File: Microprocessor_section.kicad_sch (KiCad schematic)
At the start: 17 parts, among them J9 Conn_01x04_Male, Q4 SS8050, Q5 SS8050, SW1 K2-1102SP-C4SC-04, U4 CH340C, U5 ESP32-WROOM-32D

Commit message: I was never here
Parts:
- renumbered R19 to R20, R20 to R21, R21 to R22, R22 to R23
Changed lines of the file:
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@@
   (symbol (lib_id "power:+3V3") (at 158.75 43.18 0) (unit 1)
     (in_bom yes) (on_board yes)
-    (property "Reference" "#PWR057" (id 0) (at 158.75 46.99 0)
+    (property "Reference" "#PWR058" (id 0) (at 158.75 46.99 0)
       (effects (font (size 1.27 1.27)) hide)
     )
@@
   (symbol (lib_id "power:+3V3") (at 140.97 58.42 0) (mirror y) (unit 1)
     (in_bom yes) (on_board yes)
-    (property "Reference" "#PWR055" (id 0) (at 140.97 62.23 0)
+    (property "Reference" "#PWR056" (id 0) (at 140.97 62.23 0)
       (effects (font (size 1.27 1.27)) hide)
     )
@@
   (symbol (lib_id "Device:R") (at 140.97 64.77 0) (unit 1)
     (in_bom yes) (on_board yes)
-    (property "Reference" "R22" (id 0) (at 142.748 63.6016 0)
+    (property "Reference" "R23" (id 0) (at 142.748 63.6016 0)
       (effects (font (size 1.27 1.27)) (justify left))
     )
@@
   (symbol (lib_id "power:GND") (at 158.75 60.96 0) (unit 1)
     (in_bom yes) (on_board yes)
-    (property "Reference" "#PWR058" (id 0) (at 158.75 67.31 0)
+    (property "Reference" "#PWR059" (id 0) (at 158.75 67.31 0)
       (effects (font (size 1.27 1.27)) hide)
     )
@@
   (symbol (lib_id "power:GND") (at 149.86 83.82 0) (unit 1)
     (in_bom yes) (on_board yes)
-    (property "Reference" "#PWR056" (id 0) (at 149.86 90.17 0)
+    (property "Reference" "#PWR057" (id 0) (at 149.86 90.17 0)
       (effects (font (size 1.27 1.27)) hide)
     )
@@
   (symbol (lib_id "power:+3V3") (at 33.02 166.37 0) (unit 1)
     (in_bom yes) (on_board yes)
-    (property "Reference" "#PWR047" (id 0) (at 33.02 170.18 0)
+    (property "Reference" "#PWR048" (id 0) (at 33.02 170.18 0)
       (effects (font (size 1.27 1.27)) hide)
     )
@@
   (symbol (lib_id "power:GND") (at 78.74 186.69 0) (unit 1)
     (in_bom yes) (on_board yes)
-    (property "Reference" "#PWR054" (id 0) (at 78.74 193.04 0)
+    (property "Reference" "#PWR055" (id 0) (at 78.74 193.04 0)
       (effects (font (size 1.27 1.27)) hide)
     )
@@
   (symbol (lib_id "Device:R") (at 33.02 180.34 0) (mirror x) (unit 1)
     (in_bom yes) (on_board yes)
-    (property "Reference" "R19" (id 0) (at 34.798 181.5084 0)
+    (property "Reference" "R20" (id 0) (at 34.798 181.5084 0)
       (effects (font (size 1.27 1.27)) (justify left))
     )
@@
   (symbol (lib_id "power:GND") (at 33.02 186.69 0) (unit 1)
     (in_bom yes) (on_board yes)
-    (property "Reference" "#PWR048" (id 0) (at 33.02 193.04 0)
+    (property "Reference" "#PWR049" (id 0) (at 33.02 193.04 0)
       (effects (font (size 1.27 1.27)) hide)
     )
@@
   (symbol (lib_id "power:GND") (at 177.8 137.16 0) (unit 1)
     (in_bom yes) (on_board yes)
-    (property "Reference" "#PWR059" (id 0) (at 177.8 143.51 0)
+    (property "Reference" "#PWR060" (id 0) (at 177.8 143.51 0)
       (effects (font (size 1.27 1.27)) hide)
     )
@@
   (symbol (lib_id "power:GND") (at 39.37 88.9 0) (unit 1)
     (in_bom yes) (on_board yes) (fields_autoplaced)
-    (property "Reference" "#PWR049" (id 0) (at 39.37 95.25 0)
+    (property "Reference" "#PWR050" (id 0) (at 39.37 95.25 0)
       (effects (font (size 1.27 1.27)) hide)
     )
@@
   (symbol (lib_id "power:GND") (at 64.77 101.6 0) (unit 1)
     (in_bom yes) (on_board yes) (fields_autoplaced)
-    (property "Reference" "#PWR053" (id 0) (at 64.77 107.95 0)
+    (property "Reference" "#PWR054" (id 0) (at 64.77 107.95 0)
       (effects (font (size 1.27 1.27)) hide)
     )
@@
   (symbol (lib_id "Device:R") (at 95.25 102.87 90) (unit 1)
     (in_bom yes) (on_board yes) (fields_autoplaced)
-    (property "Reference" "R21" (id 0) (at 95.25 98.1542 90))
+    (property "Reference" "R22" (id 0) (at 95.25 98.1542 90))
     (property "Value" "12k" (id 1) (at 95.25 100.6911 90))
     (property "Footprint" "Resistor_SMD:R_0603_1608Metric" (id 2) (at 95.25 104.648 90)
@@
   (symbol (lib_id "power:+3V3") (at 48.26 91.44 0) (unit 1)
     (in_bom yes) (on_board yes) (fields_autoplaced)
-    (property "Reference" "#PWR050" (id 0) (at 48.26 95.25 0)
+    (property "Reference" "#PWR051" (id 0) (at 48.26 95.25 0)
       (effects (font (size 1.27 1.27)) hide)
     )
@@
   (symbol (lib_id "power:GND") (at 48.26 101.6 0) (unit 1)
     (in_bom yes) (on_board yes) (fields_autoplaced)
-    (property "Reference" "#PWR051" (id 0) (at 48.26 107.95 0)
+    (property "Reference" "#PWR052" (id 0) (at 48.26 107.95 0)
       (effects (font (size 1.27 1.27)) hide)
     )
@@
   (symbol (lib_id "Device:R") (at 95.25 81.28 90) (unit 1)
     (in_bom yes) (on_board yes) (fields_autoplaced)
-    (property "Reference" "R20" (id 0) (at 95.25 76.5642 90))
+    (property "Reference" "R21" (id 0) (at 95.25 76.5642 90))
     (property "Value" "12k" (id 1) (at 95.25 79.1011 90))
     (property "Footprint" "Resistor_SMD:R_0603_1608Metric" (id 2) (at 95.25 83.058 90)
@@
   (symbol (lib_id "power:+3V3") (at 62.23 66.04 0) (unit 1)
     (in_bom yes) (on_board yes) (fields_autoplaced)
-    (property "Reference" "#PWR052" (id 0) (at 62.23 69.85 0)
-      (effects (font (size 1.27 1.27)) hide)
-    )
+    (property "Reference" "#PWR053" (id 0) (at 62.23 69.85 0)
+      (effects (font (size 1.27 1.27)) hide)
+    )

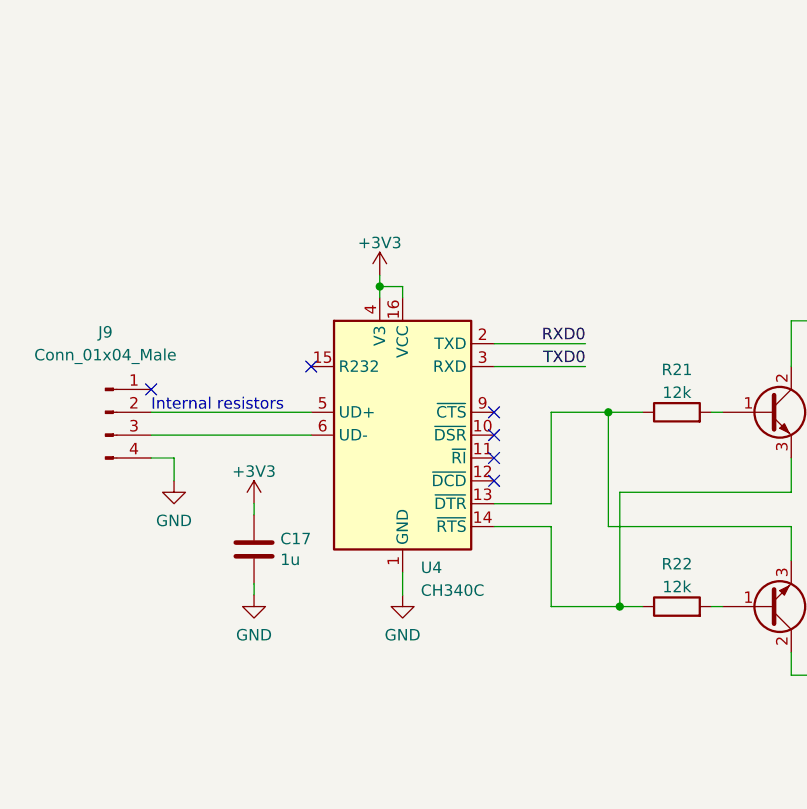
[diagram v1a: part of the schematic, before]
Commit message: Finish routing PCB revision 2
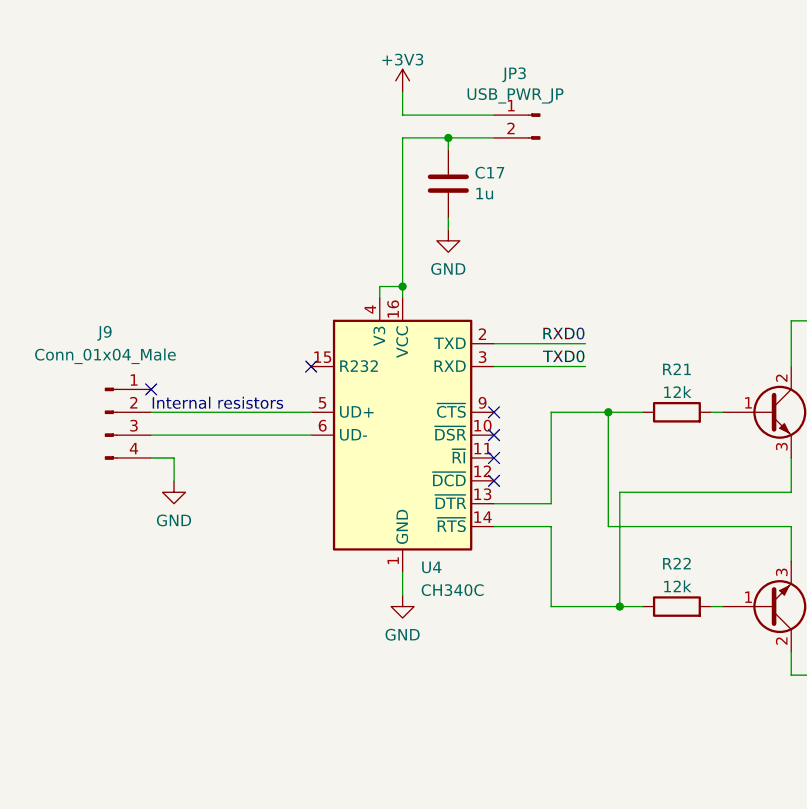
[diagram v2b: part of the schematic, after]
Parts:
- added JP3: USB_PWR_JP, Connector_PinHeader_2.54mm:PinHeader_1x02_P2.54mm_Vertical, symbol Connector:Conn_01x02_Male
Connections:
- net +3V3: now also JP3.1 (Pin_1); no longer C17.1, U4.16 (VCC), U4.4 (V3)
- new net: C17.1, JP3.2 (Pin_2), U4.16 (VCC), U4.4 (V3)
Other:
- moved on the sheet: C17
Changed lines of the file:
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@@
   (junction (at 167.64 45.72) (diameter 0) (color 0 0 0 0)
   )
-  (junction (at 62.23 67.31) (diameter 0) (color 0 0 0 0)
-  )
   (junction (at 140.97 71.12) (diameter 0) (color 0 0 0 0)
   )
@@
   )
   (junction (at 87.63 81.28) (diameter 0) (color 0 0 0 0)
+  )
+  (junction (at 69.85 50.8) (diameter 0) (color 0 0 0 0)
+  )
+  (junction (at 64.77 67.31) (diameter 0) (color 0 0 0 0)
   )
   (no_connect (at 193.04 127))
@@
     (stroke (width 0) (type default) (color 0 0 0 0))
   )
-  (wire (pts (xy 48.26 100.33) (xy 48.26 101.6))
+  (wire (pts (xy 69.85 59.69) (xy 69.85 60.96))
     (stroke (width 0) (type default) (color 0 0 0 0))
   )
@@
     (stroke (width 0) (type default) (color 0 0 0 0))
   )
+  (wire (pts (xy 74.93 50.8) (xy 69.85 50.8))
+    (stroke (width 0) (type default) (color 0 0 0 0))
+  )
+  (wire (pts (xy 69.85 50.8) (xy 64.77 50.8))
+    (stroke (width 0) (type default) (color 0 0 0 0))
+  )
   (wire (pts (xy 33.02 166.37) (xy 33.02 171.45))
     (stroke (width 0) (type default) (color 0 0 0 0))
@@
     (stroke (width 0) (type default) (color 0 0 0 0))
   )
+  (wire (pts (xy 64.77 50.8) (xy 64.77 67.31))
+    (stroke (width 0) (type default) (color 0 0 0 0))
+  )
   (wire (pts (xy 81.28 81.28) (xy 87.63 81.28))
     (stroke (width 0) (type default) (color 0 0 0 0))
   )
-  (wire (pts (xy 62.23 66.04) (xy 62.23 67.31))
-    (stroke (width 0) (type default) (color 0 0 0 0))
-  )
   (wire (pts (xy 193.04 71.12) (xy 205.74 71.12))
     (stroke (width 0) (type default) (color 0 0 0 0))
@@
     (stroke (width 0) (type default) (color 0 0 0 0))
   )
+  (wire (pts (xy 64.77 45.72) (xy 64.77 48.26))
+    (stroke (width 0) (type default) (color 0 0 0 0))
+  )
   (wire (pts (xy 193.04 111.76) (xy 205.74 111.76))
     (stroke (width 0) (type default) (color 0 0 0 0))
   )
-  (wire (pts (xy 48.26 91.44) (xy 48.26 92.71))
+  (wire (pts (xy 69.85 50.8) (xy 69.85 52.07))
     (stroke (width 0) (type default) (color 0 0 0 0))
   )
@@
   )
   (wire (pts (xy 107.95 93.98) (xy 87.63 93.98))
+    (stroke (width 0) (type default) (color 0 0 0 0))
+  )
+  (wire (pts (xy 64.77 48.26) (xy 74.93 48.26))
     (stroke (width 0) (type default) (color 0 0 0 0))
   )
@@
     (pin "2")
   )
-  (symbol (lib_id "power:+3V3") (at 48.26 91.44 0) (unit 1)
+  (symbol (lib_id "power:GND") (at 69.85 60.96 0) (unit 1)
     (in_bom yes) (on_board yes) (fields_autoplaced)
-    (property "Reference" "#PWR051" (id 0) (at 48.26 95.25 0)
-      (effects (font (size 1.27 1.27)) hide)
-    )
-    (property "Value" "+3V3" (id 1) (at 48.26 87.8642 0))
-    (property "Footprint" "" (id 2) (at 48.26 91.44 0)
-      (effects (font (size 1.27 1.27)) hide)
-    )
-    (property "Datasheet" "" (id 3) (at 48.26 91.44 0)
-      (effects (font (size 1.27 1.27)) hide)
-    )
-    (pin "1")
-  )
-  (symbol (lib_id "power:GND") (at 48.26 101.6 0) (unit 1)
-    (in_bom yes) (on_board yes) (fields_autoplaced)
-    (property "Reference" "#PWR052" (id 0) (at 48.26 107.95 0)
-      (effects (font (size 1.27 1.27)) hide)
-    )
-    (property "Value" "GND" (id 1) (at 48.26 106.0434 0))
-    (property "Footprint" "" (id 2) (at 48.26 101.6 0)
-      (effects (font (size 1.27 1.27)) hide)
-    )
-    (property "Datasheet" "" (id 3) (at 48.26 101.6 0)
-      (effects (font (size 1.27 1.27)) hide)
-    )
-    (pin "1")
-  )
-  (symbol (lib_id "Device:C") (at 48.26 96.52 0) (unit 1)
-    (in_bom yes) (on_board yes)
-    (property "Reference" "C17" (id 0) (at 51.181 95.3516 0)
-      (effects (font (size 1.27 1.27)) (justify left))
-    )
-    (property "Value" "1u" (id 1) (at 51.181 97.663 0)
-      (effects (font (size 1.27 1.27)) (justify left))
-    )
-    (property "Footprint" "Capacitor_SMD:C_0603_1608Metric" (id 2) (at 49.2252 100.33 0)
-      (effects (font (size 1.27 1.27)) hide)
-    )
-    (property "Datasheet" "~" (id 3) (at 48.26 96.52 0)
-      (effects (font (size 1.27 1.27)) hide)
-    )
-    (property "LCSC" "C15849" (id 4) (at 48.26 96.52 0)
+    (property "Reference" "#PWR052" (id 0) (at 69.85 67.31 0)
+      (effects (font (size 1.27 1.27)) hide)
+    )
+    (property "Value" "GND" (id 1) (at 69.85 65.4034 0))
+    (property "Footprint" "" (id 2) (at 69.85 60.96 0)
+      (effects (font (size 1.27 1.27)) hide)
+    )
+    (property "Datasheet" "" (id 3) (at 69.85 60.96 0)
+      (effects (font (size 1.27 1.27)) hide)
+    )
+    (pin "1")
+  )
+  (symbol (lib_id "Device:C") (at 69.85 55.88 0) (unit 1)
+    (in_bom yes) (on_board yes)
+    (property "Reference" "C17" (id 0) (at 72.771 54.7116 0)
+      (effects (font (size 1.27 1.27)) (justify left))
+    )
+    (property "Value" "1u" (id 1) (at 72.771 57.023 0)
+      (effects (font (size 1.27 1.27)) (justify left))
+    )
+    (property "Footprint" "Capacitor_SMD:C_0603_1608Metric" (id 2) (at 70.8152 59.69 0)
+      (effects (font (size 1.27 1.27)) hide)
+    )
+    (property "Datasheet" "~" (id 3) (at 69.85 55.88 0)
+      (effects (font (size 1.27 1.27)) hide)
+    )
+    (property "LCSC" "C15849" (id 4) (at 69.85 55.88 0)
       (effects (font (size 1.27 1.27)) hide)
     )
@@
     (pin "3")
     (pin "4")
+  )
+  (symbol (lib_id "Connector:Conn_01x02_Male") (at 80.01 48.26 0) (mirror y) (unit 1)
+    (in_bom yes) (on_board yes)
+    (property "Reference" "JP3" (id 0) (at 77.2668 43.6626 0))
+    (property "Value" "USB_PWR_JP" (id 1) (at 77.2668 45.974 0))
+    (property "Footprint" "Connector_PinHeader_2.54mm:PinHeader_1x02_P2.54mm_Vertical" (id 2) (at 80.01 48.26 0)
+      (effects (font (size 1.27 1.27)) hide)
+    )
+    (property "Datasheet" "~" (id 3) (at 80.01 48.26 0)
+      (effects (font (size 1.27 1.27)) hide)
+    )
+    (property "LCSC" "C160332" (id 4) (at 80.01 48.26 0)
+      (effects (font (size 1.27 1.27)) hide)
+    )
+    (pin "1")
+    (pin "2")
   )
   (symbol (lib_id "Device:R") (at 95.25 81.28 90) (unit 1)
@@
     (pin "2")
   )
-  (symbol (lib_id "power:+3V3") (at 62.23 66.04 0) (unit 1)
-    (in_bom yes) (on_board yes) (fields_autoplaced)
-    (property "Reference" "#PWR053" (id 0) (at 62.23 69.85 0)
-      (effects (font (size 1.27 1.27)) hide)
-    )
-    (property "Value" "+3V3" (id 1) (at 62.23 62.4642 0))
-    (property "Footprint" "" (id 2) (at 62.23 66.04 0)
-      (effects (font (size 1.27 1.27)) hide)
-    )
-    (property "Datasheet" "" (id 3) (at 62.23 66.04 0)
-      (effects (font (size 1.27 1.27)) hide)
-    )
+  (symbol (lib_id "power:+3V3") (at 64.77 45.72 0) (unit 1)
+    (in_bom yes) (on_board yes)
+    (property "Reference" "#PWR053" (id 0) (at 64.77 49.53 0)
+      (effects (font (size 1.27 1.27)) hide)
+    )
+    (property "Value" "+3V3" (id 1) (at 64.77 42.1442 0))
+    (property "Footprint" "" (id 2) (at 64.77 45.72 0)
+      (effects (font (size 1.27 1.27)) hide)
+    )
+    (property "Datasheet" "" (id 3) (at 64.77 45.72 0)
+      (effects (font (size 1.27 1.27)) hide)
+    )
